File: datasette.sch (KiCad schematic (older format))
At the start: 38 parts, among them CN3 CASSETTE, CN7 SERIAL_BUS, CN93 C64_STYLE_CASSETTE, J90 CONN_TAPE_DRIVE, Q5 2SD880, U9 74LS06, U91 DT1042, U92 DT1042

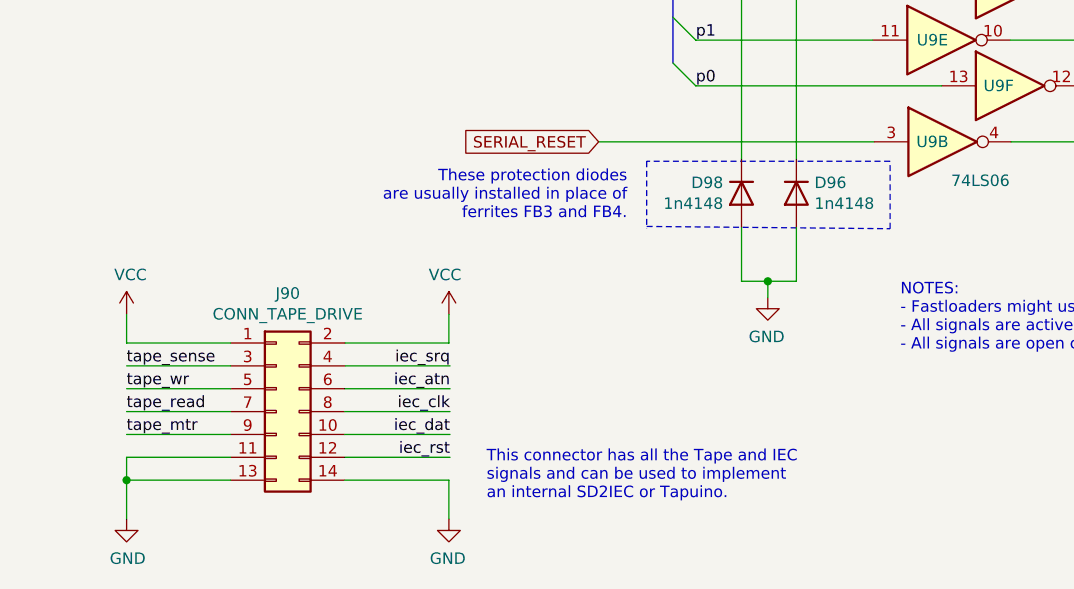
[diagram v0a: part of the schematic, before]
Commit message: Add internal IEC/TAPE headers
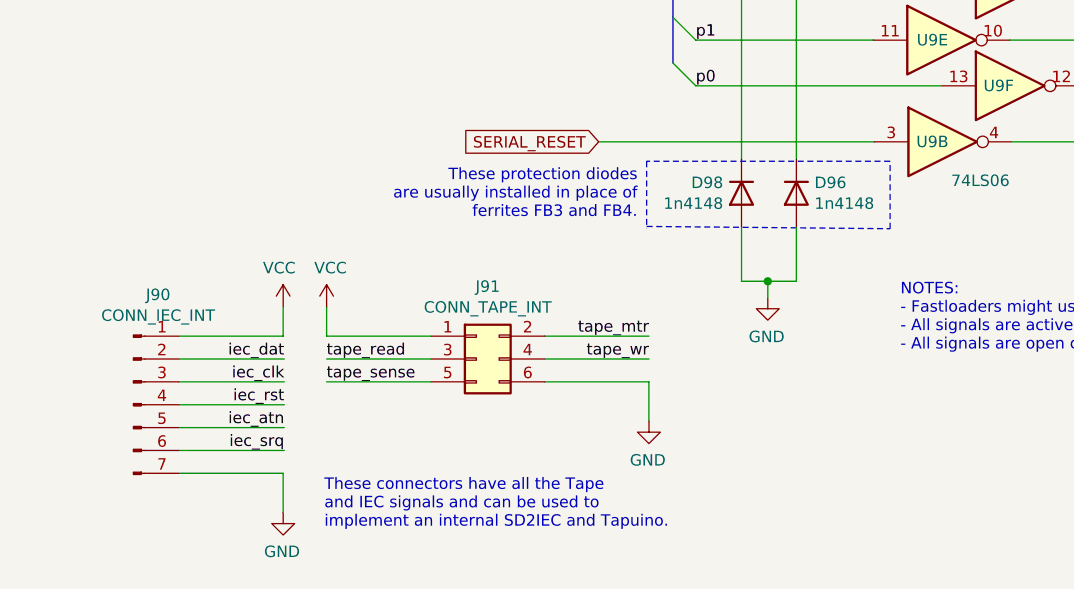
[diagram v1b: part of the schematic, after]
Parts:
- removed J90: CONN_TAPE_DRIVE, symbol Connector_Generic:Conn_02x07_Odd_Even
- added J90: CONN_IEC_INT, Connector_PinHeader_2.54mm:PinHeader_1x07_P2.54mm_Vertical, symbol Connector:Conn_01x07_Male
- added J91: CONN_TAPE_INT, Connector_PinHeader_2.54mm:PinHeader_2x03_P2.54mm_Vertical, symbol Connector_Generic:Conn_02x03_Odd_Even
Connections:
- net GND: now also J90.7 (Pin_7), J91.6 (Pin_6)
- net VCC: now also J90.1 (Pin_1), J91.1 (Pin_1)
- net iec_atn: now also J90.5 (Pin_5)
- net iec_clk: now also J90.3 (Pin_3)
- net iec_dat: now also J90.2 (Pin_2)
- net iec_rst: now also J90.4 (Pin_4)
- net iec_srq: now also J90.6 (Pin_6)
- net tape_mtr: now also J91.2 (Pin_2)
- net tape_read: now also J91.3 (Pin_3)
- net tape_sense: now also J91.5 (Pin_5)
- net tape_wr: now also J91.4 (Pin_4)
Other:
- note added: "These connectors have all the Tape\nand IEC signals and can be used to\nimplement an internal SD2IEC and Tapuino."
- note removed: "This connector has all the Tape and IEC\nsignals and can be used to implement\nan internal SD2IEC or Tapuino."
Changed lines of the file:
@@
 Sheet 7 14
 Title "LittleSixteen"
-Date "2021-12-05"
+Date "2023-07-25"
 Rev "3git"
 Comp "SukkoPera"
@@
 Wire Notes Line
 	4025 6245 4025 5950
-Text Notes 2875 6210 2    50   ~ 0
+Text Notes 2920 6205 2    50   ~ 0
 These protection diodes\nare usually installed in place of\nferrites FB3 and FB4.
 $Comp
@@
 	8925 6410 8925 2565
 Wire Wire Line
-	1140 6745 685  6745
-Wire Wire Line
-	1140 6845 685  6845
-Wire Wire Line
-	1140 6945 685  6945
-Wire Wire Line
-	1140 7045 685  7045
-Wire Wire Line
-	1140 7145 685  7145
-Wire Wire Line
-	2100 6845 1640 6845
-Wire Wire Line
-	2100 6945 1640 6945
-Wire Wire Line
-	2100 7045 1640 7045
-Wire Wire Line
-	2100 7145 1640 7145
-Wire Wire Line
-	1140 7245 685  7245
-Wire Wire Line
-	685  7245 685  7345
+	2015 6715 1560 6715
+Wire Wire Line
+	2515 6715 2970 6715
+Wire Wire Line
+	2015 6815 1560 6815
+Wire Wire Line
+	2015 6915 1560 6915
+Wire Wire Line
+	2515 6815 2970 6815
+Wire Wire Line
+	1375 6915 915  6915
+Wire Wire Line
+	1375 7015 915  7015
+Wire Wire Line
+	1375 7115 915  7115
 $Comp
 L power:GND #PWR0213
 U 1 1 623B7B36
-P 685 7515
-F 0 "#PWR0213" H 685 7265 50  0001 C CNN
-F 1 "GND" H 690 7342 50  0000 C CNN
-F 2 "" H 685 7515 50  0001 C CNN
-F 3 "" H 685 7515 50  0001 C CNN
-	1    685  7515
-	1    0    0    -1
+P 2970 7085
+F 0 "#PWR0213" H 2970 6835 50  0001 C CNN
+F 1 "GND" H 2975 6912 50  0000 C CNN
+F 2 "" H 2970 7085 50  0001 C CNN
+F 3 "" H 2970 7085 50  0001 C CNN
+	1    2970 7085
+	-1   0    0    -1
 $EndComp
 $Comp
 L power:VCC #PWR0214
 U 1 1 623B7EDA
-P 685 6620
-F 0 "#PWR0214" H 685 6470 50  0001 C CNN
-F 1 "VCC" H 702 6793 50  0000 C CNN
-F 2 "" H 685 6620 50  0001 C CNN
-F 3 "" H 685 6620 50  0001 C CNN
-	1    685  6620
+P 1560 6590
+F 0 "#PWR0214" H 1560 6440 50  0001 C CNN
+F 1 "VCC" H 1577 6763 50  0000 C CNN
+F 2 "" H 1560 6590 50  0001 C CNN
+F 3 "" H 1560 6590 50  0001 C CNN
+	1    1560 6590
 	1    0    0    -1
 $EndComp
 Text Label 5265 2425 0    50   ~ 0
 tape_mtr
-Text Label 685  6945 0    50   ~ 0
+Text Label 2970 6815 2    50   ~ 0
 tape_wr
-Text Label 685  7145 0    50   ~ 0
+Text Label 2970 6715 2    50   ~ 0
 tape_mtr
-Text Label 685  6845 0    50   ~ 0
+Text Label 1560 6915 0    50   ~ 0
 tape_sense
-Text Label 685  7045 0    50   ~ 0
+Text Label 1560 6815 0    50   ~ 0
 tape_read
-Text Label 2100 6945 2    50   ~ 0
+Text Label 1375 7115 2    50   ~ 0
 iec_atn
-Text Label 2100 7045 2    50   ~ 0
+Text Label 1375 6915 2    50   ~ 0
 iec_clk
-Text Label 2100 7145 2    50   ~ 0
+Text Label 1375 6815 2    50   ~ 0
 iec_dat
-Text Label 2100 7245 2    50   ~ 0
+Text Label 1375 7015 2    50   ~ 0
 iec_rst
 Text Label 8090 5620 1    50   ~ 0
 iec_srq
-Text Label 2100 6845 2    50   ~ 0
-iec_srq
-Wire Wire Line
-	685  6620 685  6745
-Wire Wire Line
-	1640 6745 2095 6745
+Wire Wire Line
+	1560 6590 1560 6715
+Wire Wire Line
+	915  6715 1370 6715
 $Comp
 L power:VCC #PWR0215
 U 1 1 62461BF9
-P 2095 6620
-F 0 "#PWR0215" H 2095 6470 50  0001 C CNN
-F 1 "VCC" H 2112 6793 50  0000 C CNN
-F 2 "" H 2095 6620 50  0001 C CNN
-F 3 "" H 2095 6620 50  0001 C CNN
-	1    2095 6620
-	-1   0    0    -1
-$EndComp
-Wire Wire Line
-	2095 6620 2095 6745
-$Comp
-L Connector_Generic:Conn_02x07_Odd_Even J90
-U 1 1 62482A9D
-P 1340 7045
-F 0 "J90" H 1390 7562 50  0000 C CNN
-F 1 "CONN_TAPE_DRIVE" H 1390 7471 50  0000 C CNN
-F 2 "" H 1340 7045 50  0001 C CNN
-F 3 "~" H 1340 7045 50  0001 C CNN
-	1    1340 7045
-	1    0    0    -1
-$EndComp
-Wire Wire Line
-	1140 7345 685  7345
-Connection ~ 685  7345
-Wire Wire Line
-	685  7345 685  7515
+P 1370 6590
+F 0 "#PWR0215" H 1370 6440 50  0001 C CNN
+F 1 "VCC" H 1387 6763 50  0000 C CNN
+F 2 "" H 1370 6590 50  0001 C CNN
+F 3 "" H 1370 6590 50  0001 C CNN
+	1    1370 6590
+	-1   0    0    -1
+$EndComp
+Wire Wire Line
+	1370 6590 1370 6715
+Wire Wire Line
+	2515 6915 2970 6915
+Wire Wire Line
+	2970 6915 2970 7085
 $Comp
 L power:GND #PWR0216
 U 1 1 624971E6
-P 2095 7515
-F 0 "#PWR0216" H 2095 7265 50  0001 C CNN
-F 1 "GND" H 2100 7342 50  0000 C CNN
-F 2 "" H 2095 7515 50  0001 C CNN
-F 3 "" H 2095 7515 50  0001 C CNN
-	1    2095 7515
-	-1   0    0    -1
-$EndComp
-Wire Wire Line
-	1640 7345 2095 7345
-Wire Wire Line
-	2095 7345 2095 7515
-Wire Wire Line
-	1640 7245 2100 7245
-Text Notes 2260 7435 0    50   ~ 0
-This connector has all the Tape and IEC\nsignals and can be used to implement\nan internal SD2IEC or Tapuino.
+P 1370 7485
+F 0 "#PWR0216" H 1370 7235 50  0001 C CNN
+F 1 "GND" H 1375 7312 50  0000 C CNN
+F 2 "" H 1370 7485 50  0001 C CNN
+F 3 "" H 1370 7485 50  0001 C CNN
+	1    1370 7485
+	-1   0    0    -1
+$EndComp
+Wire Wire Line
+	915  7315 1370 7315
+Wire Wire Line
+	1370 7315 1370 7485
+Wire Wire Line
+	915  7215 1375 7215
 Wire Wire Line
 	7430 5820 7430 6085
@@
 Text Label 7915 2425 0    50   ~ 0
 tape_mtr2
+$Comp
+L Connector:Conn_01x07_Male J90
+U 1 1 64DB182D
+P 715 7015
+F 0 "J90" H 823 7496 50  0000 C CNN
+F 1 "CONN_IEC_INT" H 823 7405 50  0000 C CNN
+F 2 "Connector_PinHeader_2.54mm:PinHeader_1x07_P2.54mm_Vertical" H 715 7015 50  0001 C CNN
+F 3 "~" H 715 7015 50  0001 C CNN
+	1    715  7015
+	1    0    0    -1
+$EndComp
+$Comp
+L Connector_Generic:Conn_02x03_Odd_Even J91
+U 1 1 64DC3929
+P 2215 6815
+F 0 "J91" H 2265 7132 50  0000 C CNN
+F 1 "CONN_TAPE_INT" H 2265 7041 50  0000 C CNN
+F 2 "Connector_PinHeader_2.54mm:PinHeader_2x03_P2.54mm_Vertical" H 2215 6815 50  0001 C CNN
+F 3 "~" H 2215 6815 50  0001 C CNN
+	1    2215 6815
+	1    0    0    -1
+$EndComp
+Text Label 1375 7215 2    50   ~ 0
+iec_srq
+Wire Wire Line
+	1375 6815 915  6815
 Wire Bus Line
 	3075 4640 3075 5520
+Text Notes 1550 7560 0    50   ~ 0
+These connectors have all the Tape\nand IEC signals and can be used to\nimplement an internal SD2IEC and Tapuino.
 $EndSCHEMATC

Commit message: Rationalize BOM There should be no significant changes on both schematics on PCB, just some values and something on the silkscreen
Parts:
- removed FB1, FB19, FB2, FB3, FB4, FB5: Ferrite_3pin, LittleSixteen:Ferrite, symbol Ferrite3Pin:Ferrite_3pin
- added FB1, FB19, FB2, FB3, FB4, FB5: DSS1NB32A271Q91A, LittleSixteen:EMI_Filter, symbol emi_filter_3pin:EMI_Filter_3Pin
- C23, C24, C25: MouserPN (none) -> 810-FG28C0G1H471JNT6
- C26: MouserPN (none) -> 810-FG28X7R1H104KNT0
- FB14, FB15, FB16, FB17, FB18: value Ferrite_Bead_Small -> DSS1NB32A271Q91A; footprint LittleSixteen:Ferrite -> LittleSixteen:EMI_Filter; symbol ferrite_bead_small:Ferrite_Bead_Small -> emi_filter_3pin:EMI_Filter_3Pin
- R94: value 4.7R 1W -> 4.7 1W
- RP1: Notes (none) -> Bussed
- U92: Notes Optional, protects Serial port from ESD -> Optional, protects Tape port from ESD
- renumbered J90 to CN15, J91 to CN16
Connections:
- net GND: now also FB1.2, FB1.3 (GND), FB19.3 (GND), FB2.3 (GND), FB3.3 (GND), FB4.3 (GND), FB5.3 (GND)
- net iec_atn: now also FB5.1
- net iec_clk: now also FB4.1
- net iec_dat: now also FB3.1
- net iec_rst: now also FB2.1
- net p7: now also FB3.2
- net p[0..7]: now also FB4.2
- net tape_mtr: now also FB19.1
- net tape_mtr2: now also FB19.2
- net ~ATTN: now also FB5.2
- net ~BRESET: now also FB2.2
- net at CN7.2: now also FB1.1

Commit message: Rationalize capacitor footprints & BOM
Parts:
- CN93: MouserPN (none) -> ---
- R29: MouserPN (none) -> 708-RNF14FTD100R
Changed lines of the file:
@@
 F 2 "Resistor_THT:R_Axial_DIN0207_L6.3mm_D2.5mm_P5.08mm_Vertical" V 6355 2325 50  0001 C CNN
 F 3 "~" H 6425 2325 50  0001 C CNN
+F 4 "708-RNF14FTD100R" H 6425 2325 50  0001 C CNN "MouserPN"
 	1    6425 2325
 	0    -1   -1   0
@@
 F 2 "LittleSixteen:C64-Cassette-Port-Male" H 1570 3135 50  0001 C CNN
 F 3 "~" H 1570 3135 50  0001 C CNN
+F 4 "---" H 1570 3135 50  0001 C CNN "MouserPN"
 	1    1570 3135
 	-1   0    0    1

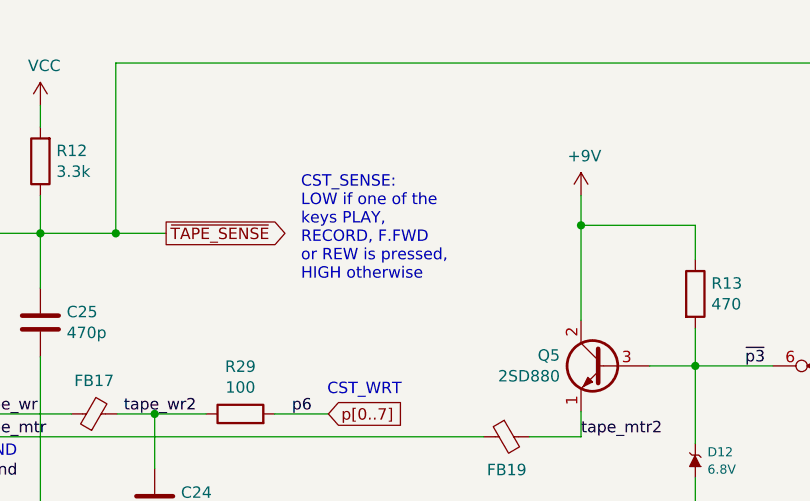
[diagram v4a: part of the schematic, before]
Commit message: Add a note about datassette Sense This led to https://github.com/sweetlilmre/tapuino/pull/52
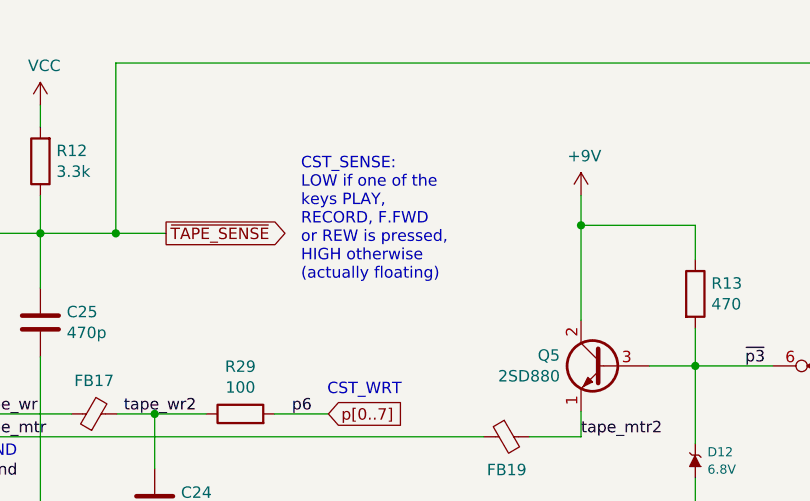
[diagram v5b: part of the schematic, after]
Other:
- note added: "CST_SENSE:\nLOW if one of the\nkeys PLAY,\nRECORD, F.FWD\nor REW is pressed,\nHIGH otherwise\n(actually floating)"
- note removed: "CST_SENSE:\nLOW if one of the\nkeys PLAY,\nRECORD, F.FWD\nor REW is pressed,\nHIGH otherwise"
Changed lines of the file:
@@
 Sheet 7 14
 Title "LittleSixteen"
-Date "2023-07-25"
+Date "2024-07-21"
 Rev "4git"
 Comp "SukkoPera"
@@
 	5880 1535 6100 1535
 Text Notes 6690 1745 0    50   ~ 0
-CST_SENSE:\nLOW if one of the\nkeys PLAY,\nRECORD, F.FWD\nor REW is pressed,\nHIGH otherwise
+CST_SENSE:\nLOW if one of the\nkeys PLAY,\nRECORD, F.FWD\nor REW is pressed,\nHIGH otherwise\n(actually floating)
 Text GLabel 6100 1535 2    50   Output ~ 0
 ~TAPE_SENSE

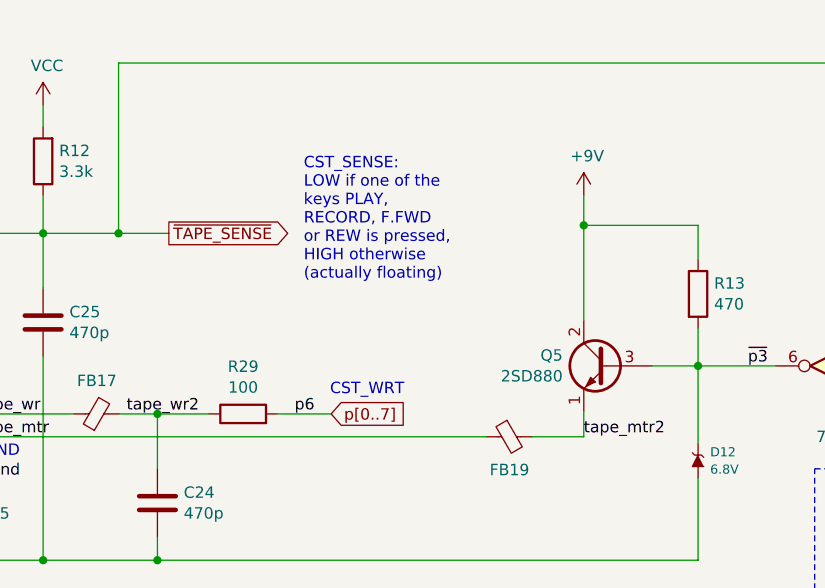
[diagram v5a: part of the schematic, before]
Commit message: Add P7 option for Tape Sense jumper, in order to replicate Plus/4 J8/J9
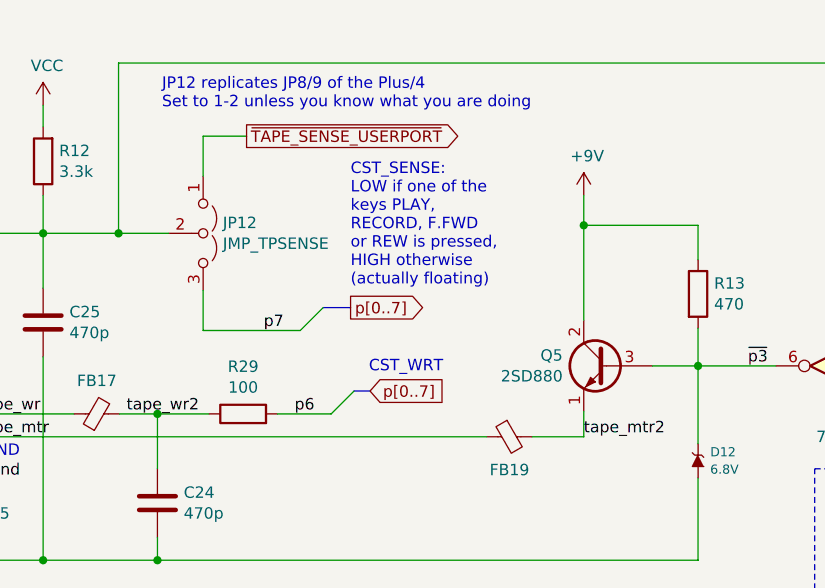
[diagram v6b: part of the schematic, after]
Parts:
- added JP12: JMP_TPSENSE, Connector_PinHeader_2.54mm:PinHeader_1x03_P2.54mm_Vertical, symbol Jumper:Jumper_3_Open
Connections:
- net p7: now also JP12.3 (B)
- net p[0..7]: no longer D96.1 (K), D97.2 (A), FB4.2, R29.2, RP1.5 (R4.2), U9.10
- net ~TAPE_SENSE: no longer names the net of C25.2, D93.1 (K), FB18.2, R12.1
- net ~TAPE_SENSE: now also JP12.2 (C)
- new net p6: D96.1 (K), D97.2 (A), FB4.2, R29.2, RP1.5 (R4.2), U9.10
- new net ~TAPE_SENSE_USERPORT: JP12.1 (A)
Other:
- note added: "JP12 replicates JP8/9 of the Plus/4\nSet to 1-2 unless you know what you are doing"
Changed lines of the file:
@@
 Sheet 7 14
 Title "LittleSixteen"
-Date "2024-07-21"
+Date "2024-08-07"
 Rev "4git"
 Comp "SukkoPera"
@@
 Wire Wire Line
 	6050 2865 6050 2965
-Wire Wire Line
-	6575 2325 6810 2325
 $Comp
 L Device:C C25
@@
 Wire Wire Line
 	5550 975  5550 1070
-Text GLabel 6810 2325 2    50   Input ~ 0
-p[0..7]
-Text Label 6650 2325 0    50   ~ 0
-p6
 Text GLabel 9940 2115 2    50   Input ~ 0
 p[0..7]
@@
 Text Notes 2405 1110 0    157  ~ 0
 DATASSETTE\nINTERFACE
-Text Notes 7130 2250 2    50   ~ 0
+Text Notes 7300 2150 2    50   ~ 0
 CST_WRT
 Wire Wire Line
@@
 Wire Wire Line
 	5880 1535 6100 1535
-Text Notes 6690 1745 0    50   ~ 0
+Text Notes 6895 1770 0    50   ~ 0
 CST_SENSE:\nLOW if one of the\nkeys PLAY,\nRECORD, F.FWD\nor REW is pressed,\nHIGH otherwise\n(actually floating)
-Text GLabel 6100 1535 2    50   Output ~ 0
-~TAPE_SENSE
+Text GLabel 6440 1110 2    50   Output ~ 0
+~TAPE_SENSE_USERPORT
 $Comp
 L Device:R_Network05_Split RP1
@@
 Wire Wire Line
 	7430 6085 7965 6085
+$Comp
+L Jumper:Jumper_3_Open JP12
+U 1 1 66B76798
+P 6250 1535
+F 0 "JP12" V 6204 1621 50  0000 L CNN
+F 1 "JMP_TPSENSE" V 6295 1621 50  0000 L CNN
+F 2 "Connector_PinHeader_2.54mm:PinHeader_1x03_P2.54mm_Vertical" H 6250 1535 50  0001 C CNN
+F 3 "~" H 6250 1535 50  0001 C CNN
+	1    6250 1535
+	0    1    1    0
+$EndComp
+Wire Wire Line
+	6250 1285 6250 1110
+Wire Wire Line
+	6250 1110 6440 1110
+Wire Wire Line
+	6250 1785 6250 1960
+Text Notes 6070 995  0    50   ~ 0
+JP12 replicates JP8/9 of the Plus/4\nSet to 1-2 unless you know what you are doing
+Text Label 6650 2325 0    50   ~ 0
+p6
+Text GLabel 6980 2225 2    50   Input ~ 0
+p[0..7]
+Wire Wire Line
+	6575 2325 6810 2325
+Text Label 6515 1960 0    50   ~ 0
+p7
+Text GLabel 6895 1860 2    50   Output ~ 0
+p[0..7]
+Wire Wire Line
+	6250 1960 6675 1960
+Entry Wire Line
+	6810 2325 6910 2225
+Wire Bus Line
+	6910 2225 6980 2225
+Entry Wire Line
+	6675 1960 6775 1860
+Wire Bus Line
+	6775 1860 6895 1860
 Wire Bus Line
 	3075 4640 3075 5520
